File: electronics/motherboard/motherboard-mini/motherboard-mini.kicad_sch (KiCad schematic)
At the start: 44 parts, among them J1 JTAG, J12 JTAG, J3 2604-3102, J5 USB4145-03-0230-C, Q1 MMDT3904, Q2 BC847, SW1 BOOT, SW2 RESET, U1 CP2102N-Axx-xQFN28, U2 ESP32-WROOM-32E_(16MB), Y1 32.768KHz

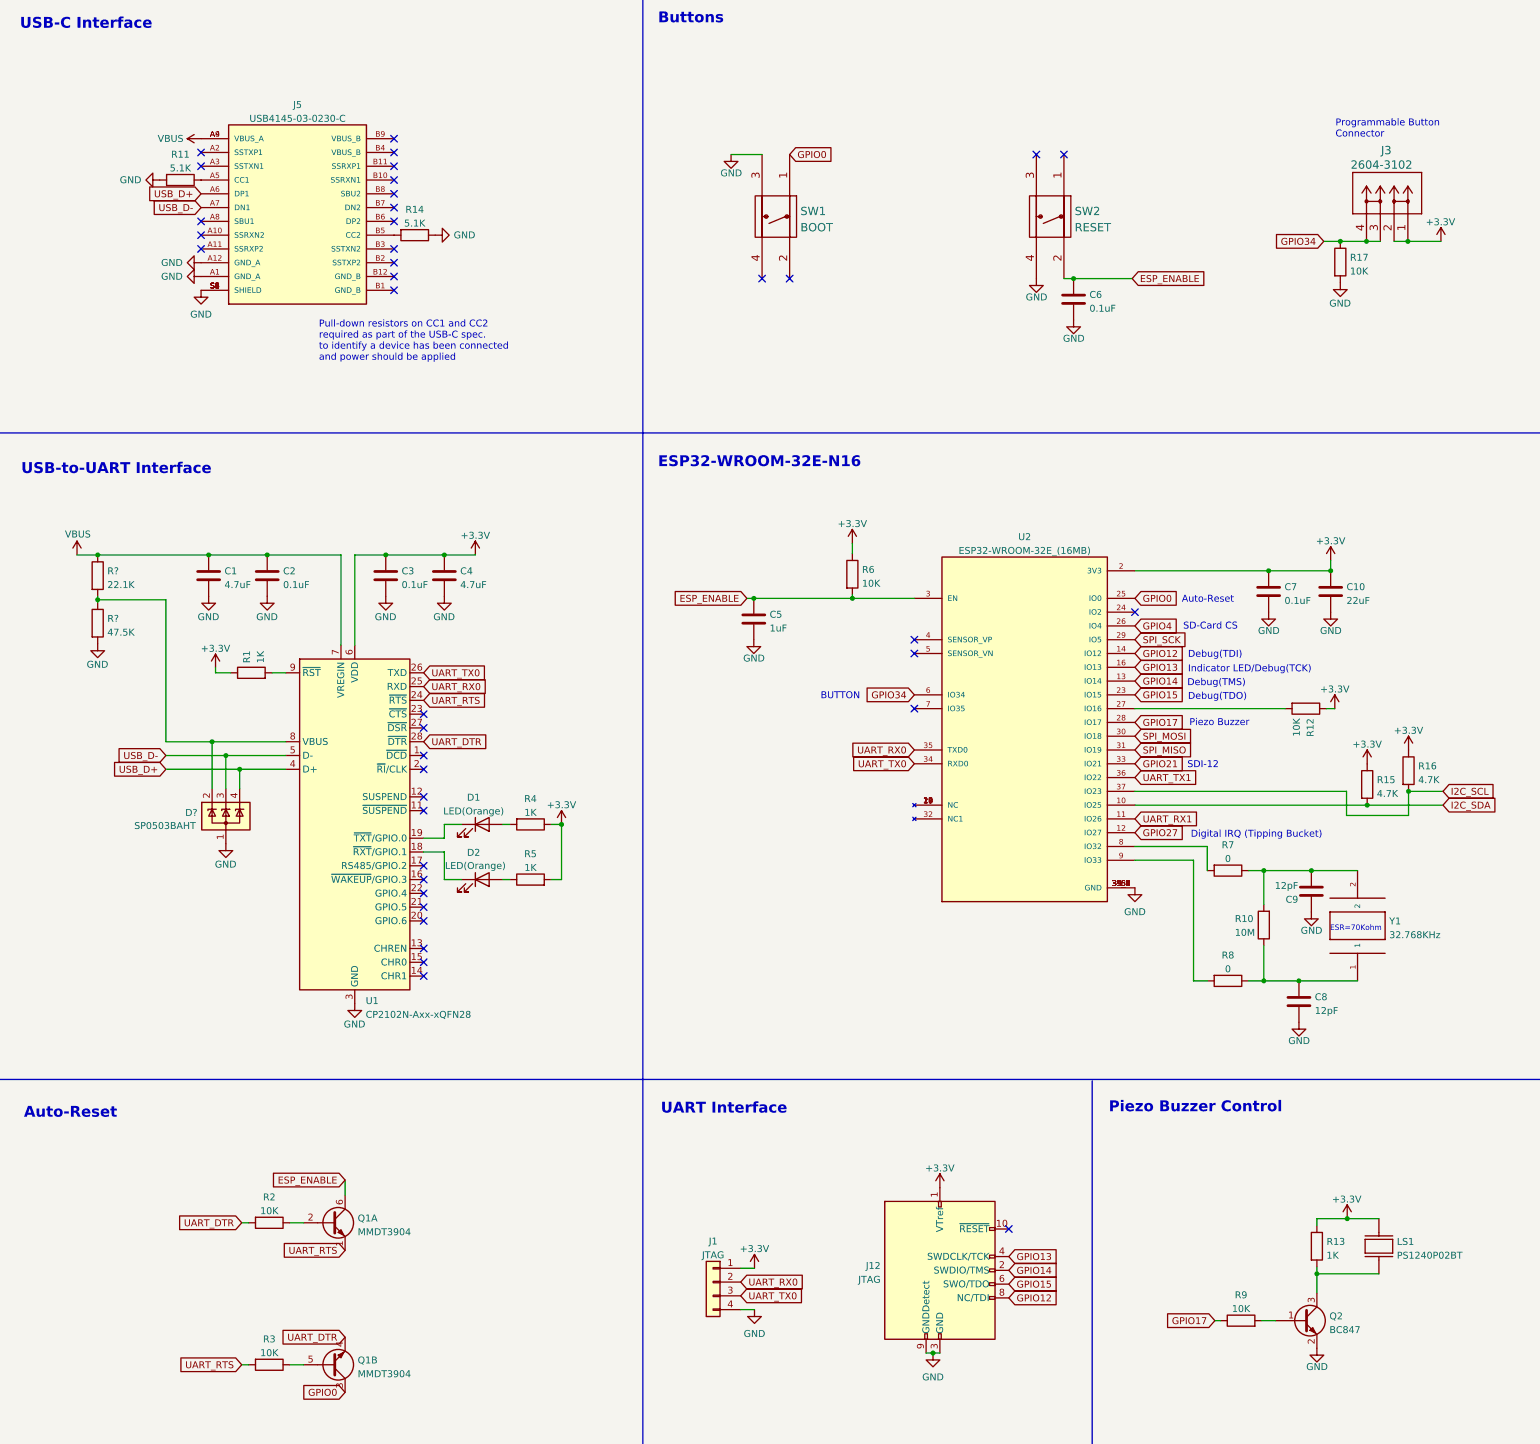
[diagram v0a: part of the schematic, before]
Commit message: new version sent for manufacture, updated component positioning, removed level shifter on SDI-12 line, re routed the solar charge circuit
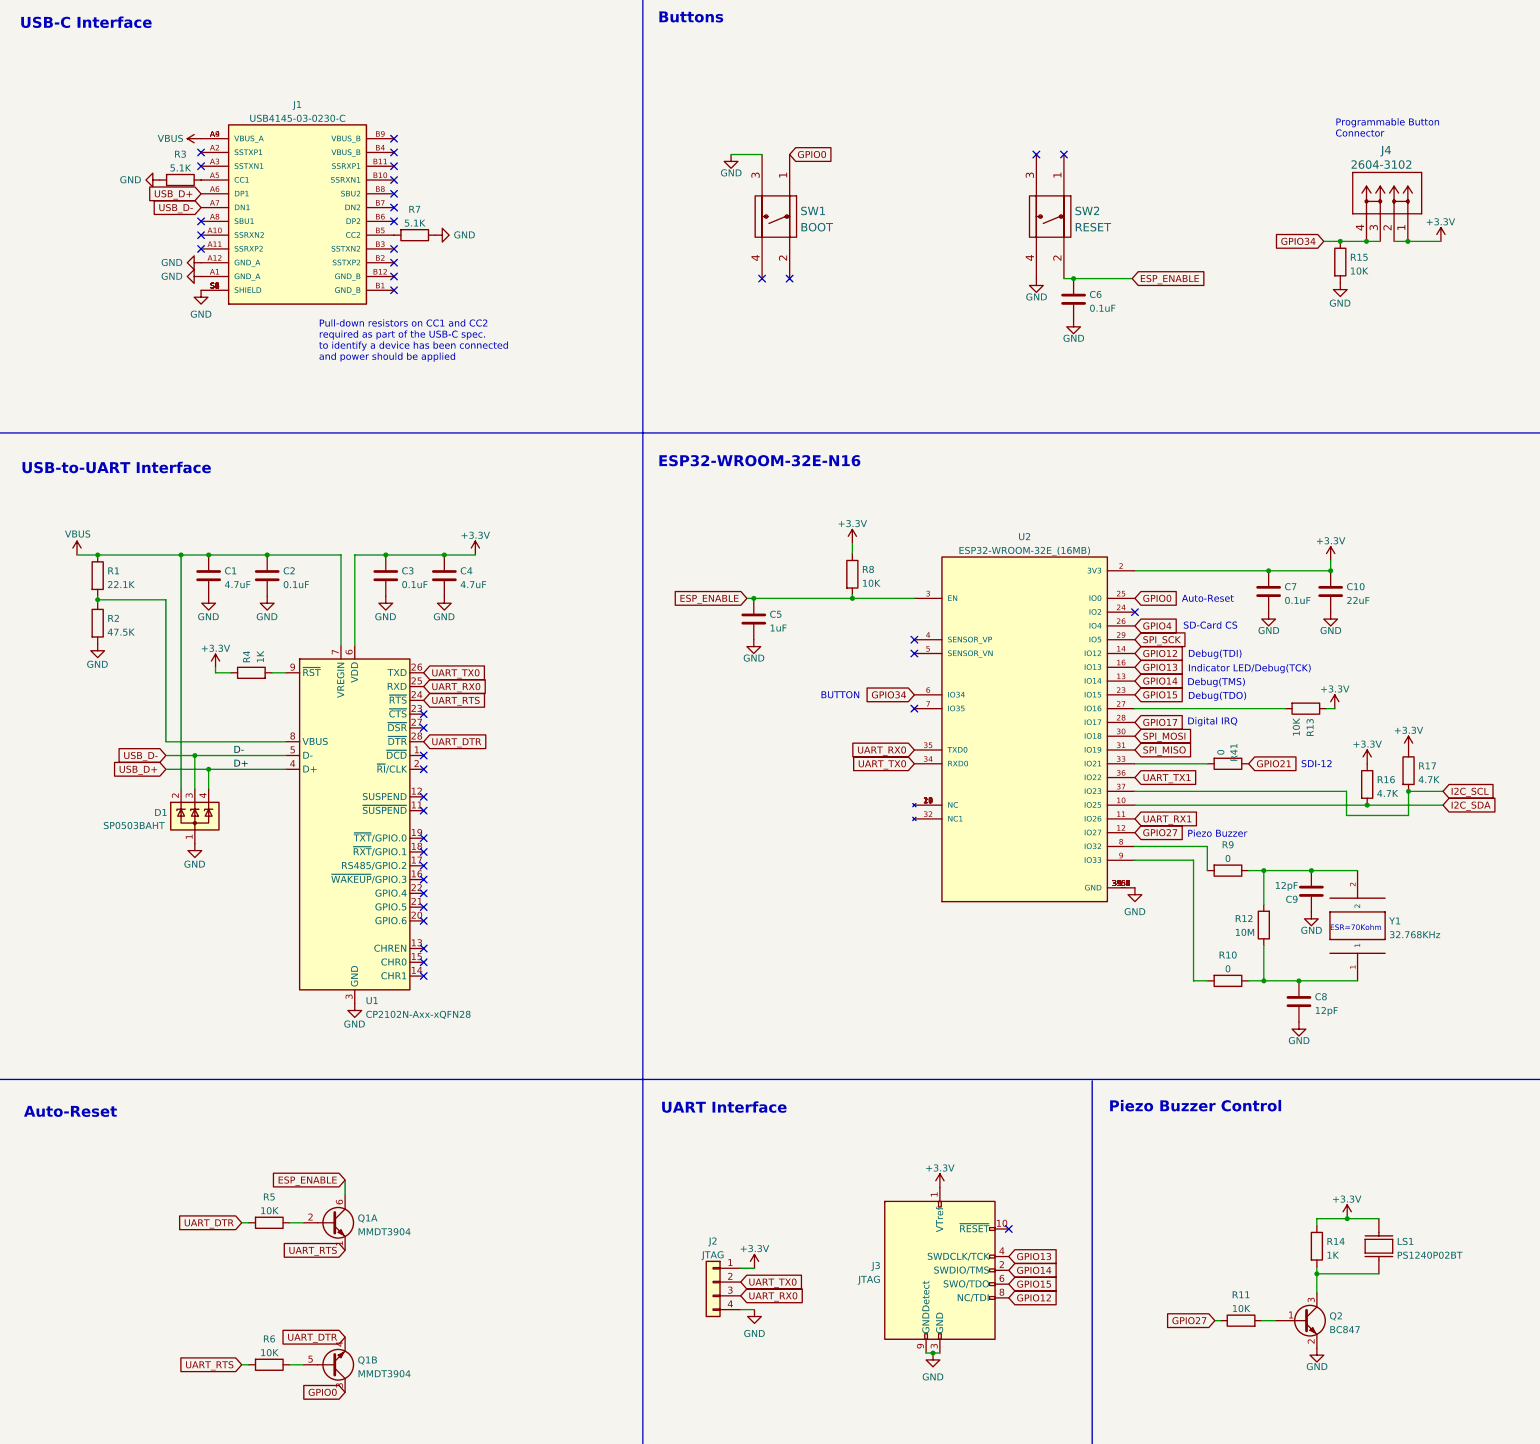
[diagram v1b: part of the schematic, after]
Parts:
- removed D1, D2: LED(Orange), LED_SMD:LED_0805_2012Metric, symbol Device:LED
- removed R4, R5: 1K, Resistor_SMD:R_0805_2012Metric, symbol Device:R
- added R41: 0, Resistor_SMD:R_0805_2012Metric, symbol Device:R
- gave numbers to parts that had none: 3
- renumbered J5 to J1, J1 to J2, J12 to J3, J3 to J4, R8 to R10, R9 to R11, R10 to R12, R12 to R13, R13 to R14, R17 to R15, R15 to R16, R16 to R17, R11 to R3, R1 to R4, R2 to R5, R3 to R6, R14 to R7, R6 to R8, R7 to R9
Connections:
- net GPIO17: no longer R11.1
- net GPIO21: now also R41.1; no longer U2.33 (IO21)
- net GPIO27: now also R11.1
- net UART_RX0: now also J2.3 (Pin_3); no longer J2.2 (Pin_2)
- net UART_TX0: now also J2.2 (Pin_2); no longer J2.3 (Pin_3)
- net VBUS: now also D1.2 (K)
- net at R1.2, R2.1, U1.8 (VBUS): no longer D1.2 (K)
- new net: R41.2, U2.33 (IO21)
- no-connect marks 39 -> 41
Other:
- note added: "Digital IRQ"
- note removed: "Digital IRQ (Tipping Bucket)"
- moved on the sheet: D1

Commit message: refactored schemematics and added pdf previews for readme
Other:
- company: (none) -> NSW Department of Primary Industries
- title: (none) -> Enviro-node
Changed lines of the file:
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@@
 (kicad_sch (version 20211123) (generator eeschema)
   (paper "A3")
+  (title_block
+    (title "Enviro-node")
+    (date "2023-01-09")
+    (rev "1.0")
+    (company "NSW Department of Primary Industries")
+    (comment 1 "GitHub: https://github.com/DPIclimate/enviro-node")
+    (comment 2 "Designed by: Harvey Bates")
+  )
   (junction (at 252.73 194.945) (diameter 0) (color 0 0 0 0)
   )
